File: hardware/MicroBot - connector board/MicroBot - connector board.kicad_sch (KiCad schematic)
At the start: 29 parts, among them J0 SMM_Mega_Shield_Connector, J1 X_Axis_Stepper_Controller, J3 gen4-IB, J4 24VDC, M1 Motor_DC, U1 L9110_H-Bridge, U2 R-78C12-1.0, U3 R-78C12-1.0, U5 OKI-78SR-5_1.5-W36-C

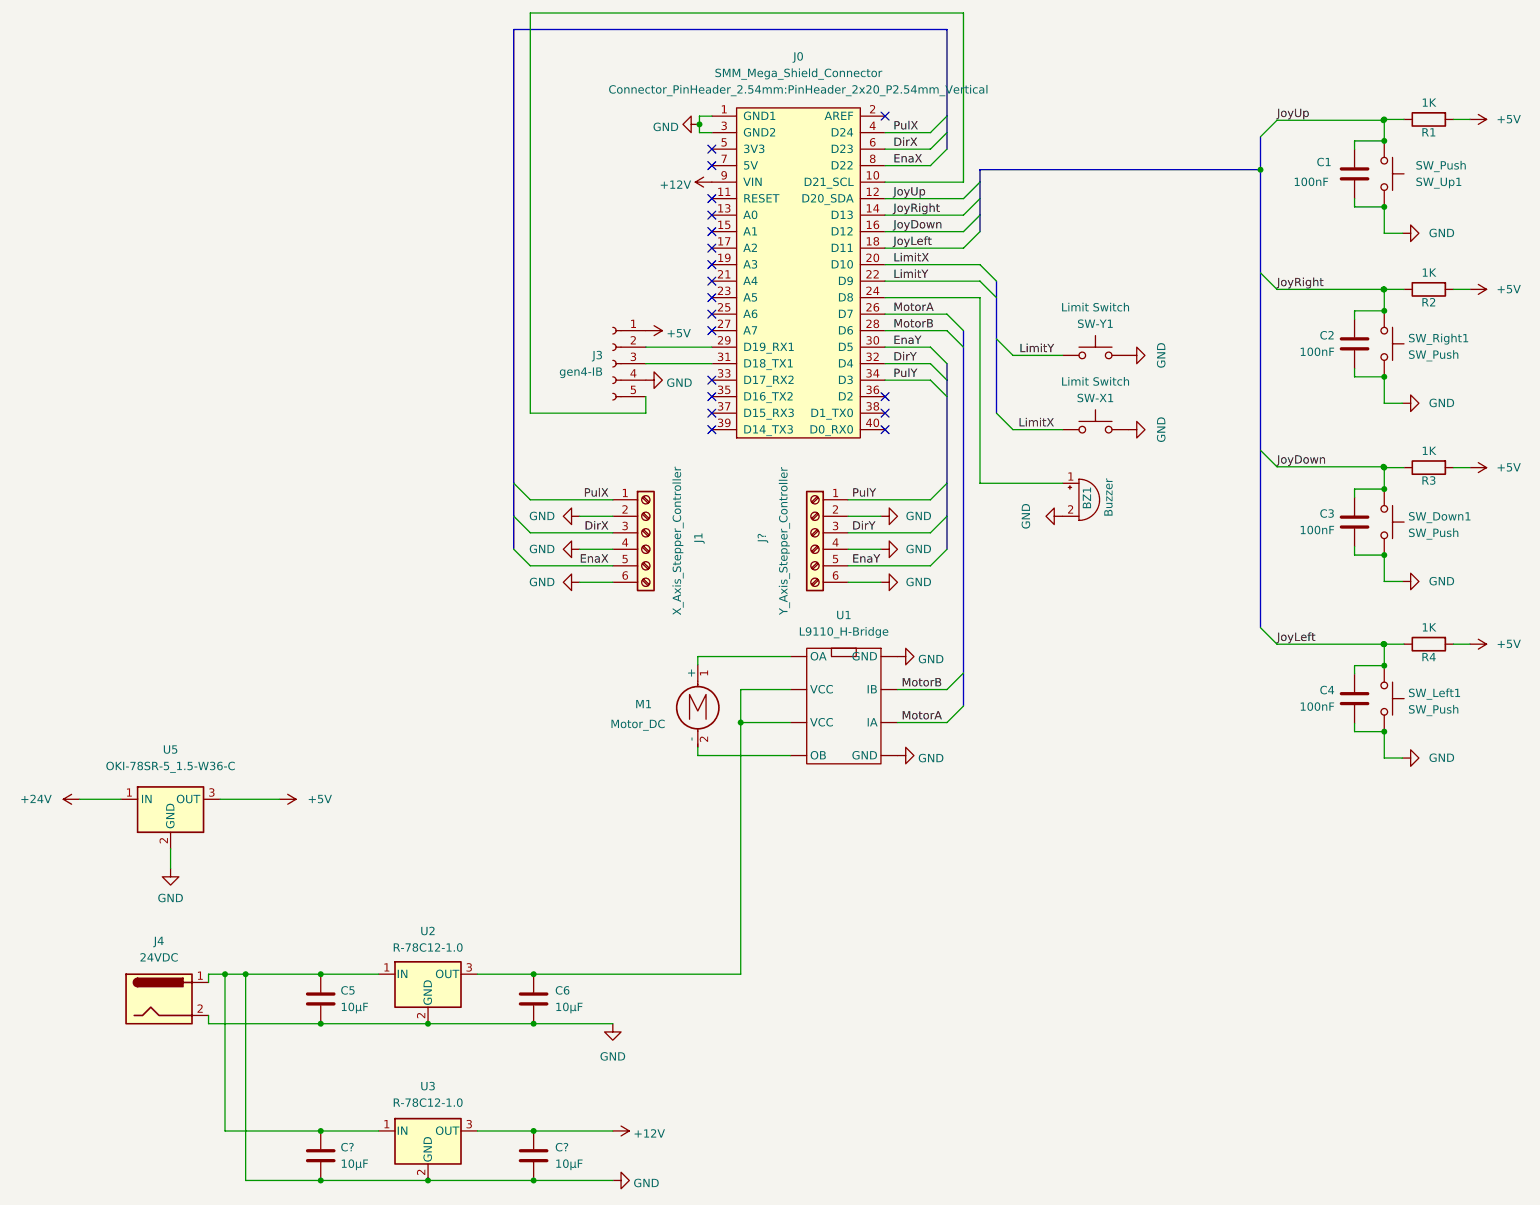
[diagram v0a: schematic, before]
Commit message: add first-pass PCB layout
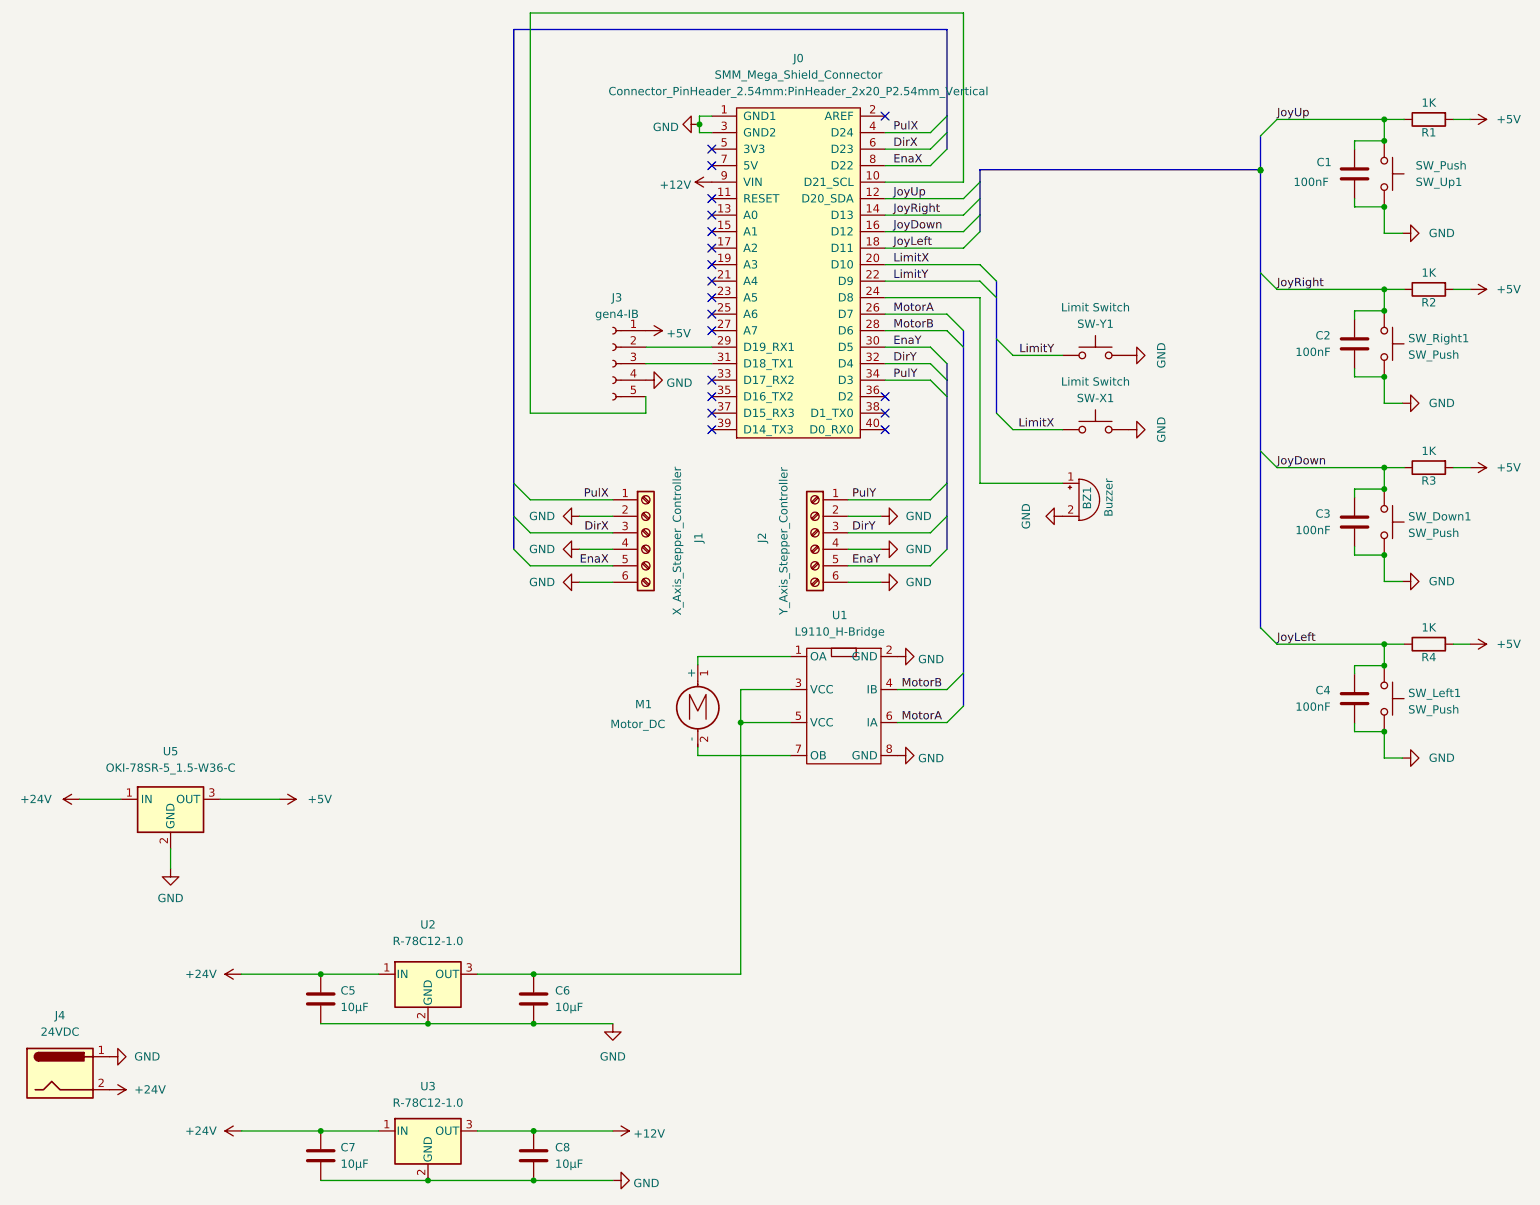
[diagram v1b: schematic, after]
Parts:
- C1, C2, C3, C4: footprint Capacitor_THT:CP_Radial_D4.0mm_P1.50mm -> Capacitor_THT:C_Disc_D3.0mm_W2.0mm_P2.50mm
- J1: footprint (none) -> TerminalBlock:TerminalBlock_bornier-6_P5.08mm
- J2: renamed from J?; footprint (none) -> TerminalBlock:TerminalBlock_bornier-6_P5.08mm
- J3: footprint SMM:I50115 -> Connector_PinSocket_2.54mm:PinSocket_1x05_P2.54mm_Horizontal
- U1: footprint Package_DIP:DIP-8-16_W7.62mm_Socket -> Package_DIP:DIP-8_W7.62mm_Socket
- gave numbers to parts that had none: 2
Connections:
- net +24V: now also C5.1, C7.1, J4.2, U2.1 (IN), U3.1 (IN)
- net GND: now also U1.2 (GND), U1.8 (GND); no longer C5.1, C7.1, J4.2, U1. (VCC), U2.1 (IN), U3.1 (IN)
- net JoyDown: now also C3.2, R3.1, SW_Down1.2
- net JoyLeft: now also C4.2, R4.1, SW_Left1.2
- net JoyRight: now also C2.2, R2.1, SW_Right1.2
- net JoyUp: now also C1.2, R1.1, SW_Up1.2
- net MotorA: now also U1.6 (IA); no longer U1. (VCC)
- net MotorB: now also U1.4 (IB); no longer U1. (VCC)
- net at M1.1 (+): now also U1.1 (OA); no longer U1. (VCC)
- net at M1.2 (-): now also U1.7 (OB); no longer U1. (VCC)
- net at C6.1, U2.3 (OUT): now also U1.3 (VCC), U1.5 (VCC); no longer U1. (VCC)
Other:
- moved on the sheet: J4

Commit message: finalize board layout
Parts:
- added D1: LED, SMM:LED_D3.0mm, symbol Device:LED
- added R5: R, SMM:Resistor_L6.3mm_D2.5mm_P10.16mm_Horizontal, symbol Device:R
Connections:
- net +5V: now also D1.2 (A)
- net GND: now also R5.2
- new net: D1.1 (K), R5.1
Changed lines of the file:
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@@
+    (pin "2")
+  )
+  (symbol (lib_id "Device:LED") (at 177.927 137.795 90) (unit 1)
+    (in_bom yes) (on_board yes) (fields_autoplaced)
+    (property "Reference" "D1" (id 0) (at 181.61 138.1124 90)
+      (effects (font (size 1.27 1.27)) (justify right))
+    )
+    (property "Value" "LED" (id 1) (at 181.61 140.6524 90)
+      (effects (font (size 1.27 1.27)) (justify right))
+    )
+    (property "Footprint" "SMM:LED_D3.0mm" (id 2) (at 177.927 137.795 0)
+      (effects (font (size 1.27 1.27)) hide)
+    )
+    (property "Datasheet" "~" (id 3) (at 177.927 137.795 0)
+      (effects (font (size 1.27 1.27)) hide)
+    )
+    (pin "1")
     (pin "2")
   )
@@
     )
     (property "Datasheet" "" (id 3) (at 149.225 103.505 0)
+      (effects (font (size 1.27 1.27)) hide)
+    )
+    (pin "1")
+  )
+  (symbol (lib_id "power:GND") (at 177.927 149.225 0) (unit 1)
+    (in_bom yes) (on_board yes) (fields_autoplaced)
+    (property "Reference" "#PWR016" (id 0) (at 177.927 155.575 0)
+      (effects (font (size 1.27 1.27)) hide)
+    )
+    (property "Value" "GND" (id 1) (at 177.927 153.67 0))
+    (property "Footprint" "" (id 2) (at 177.927 149.225 0)
+      (effects (font (size 1.27 1.27)) hide)
+    )
+    (property "Datasheet" "" (id 3) (at 177.927 149.225 0)
       (effects (font (size 1.27 1.27)) hide)
     )
@@
     (pin "2")
   )
+  (symbol (lib_id "power:+5V") (at 177.927 133.985 0) (unit 1)
+    (in_bom yes) (on_board yes) (fields_autoplaced)
+    (property "Reference" "#PWR015" (id 0) (at 177.927 137.795 0)
+      (effects (font (size 1.27 1.27)) hide)
+    )
+    (property "Value" "+5V" (id 1) (at 177.927 128.27 0))
+    (property "Footprint" "" (id 2) (at 177.927 133.985 0)
+      (effects (font (size 1.27 1.27)) hide)
+    )
+    (property "Datasheet" "" (id 3) (at 177.927 133.985 0)
+      (effects (font (size 1.27 1.27)) hide)
+    )
+    (pin "1")
+  )
   (symbol (lib_id "Connector:Screw_Terminal_01x06") (at 113.03 95.885 0) (unit 1)
     (in_bom yes) (on_board yes)
@@
     (pin "1")
   )
+  (symbol (lib_id "Device:R") (at 177.927 145.415 0) (unit 1)
+    (in_bom yes) (on_board yes) (fields_autoplaced)
+    (property "Reference" "R5" (id 0) (at 180.34 144.1449 0)
+      (effects (font (size 1.27 1.27)) (justify left))
+    )
+    (property "Value" "R" (id 1) (at 180.34 146.6849 0)
+      (effects (font (size 1.27 1.27)) (justify left))
+    )
+    (property "Footprint" "SMM:Resistor_L6.3mm_D2.5mm_P10.16mm_Horizontal" (id 2) (at 176.149 145.415 90)
+      (effects (font (size 1.27 1.27)) hide)
+    )
+    (property "Datasheet" "~" (id 3) (at 177.927 145.415 0)
+      (effects (font (size 1.27 1.27)) hide)
+    )
+    (pin "1")
+    (pin "2")
+  )
   (symbol (lib_id "power:GND") (at 229.489 75.946 90) (mirror x) (unit 1)
     (in_bom yes) (on_board yes) (fields_autoplaced)
@@
       (reference "#PWR014") (unit 1) (value "GND") (footprint "")
     )
+    (path "/c90f9f6a-5ba5-4e90-a36c-e181972e485f"
+      (reference "#PWR015") (unit 1) (value "+5V") (footprint "")
+    )
+    (path "/15186413-bac9-4c4a-a393-6697a203cfc2"
+      (reference "#PWR016") (unit 1) (value "GND") (footprint "")
+    )
     (path "/2d62c43b-bbf2-4b5c-8cbd-bda299b98654"
       (reference "#PWR0101") (unit 1) (value "+5V") (footprint "")
@@
       (reference "C8") (unit 1) (value "10µF") (footprint "Capacitor_THT:CP_Radial_D4.0mm_P1.50mm")
     )
+    (path "/0fedbe39-d937-427c-8b3c-c6565775d49f"
+      (reference "D1") (unit 1) (value "LED") (footprint "SMM:LED_D3.0mm")
+    )
     (path "/8cf7d650-0997-40ed-ba86-7eb9a2ea678a"
       (reference "J0") (unit 1) (value "SMM_Mega_Shield_Connector") (footprint "Connector_PinHeader_2.54mm:PinHeader_2x20_P2.54mm_Vertical")
@@
       (reference "R4") (unit 1) (value "1K") (footprint "SMM:Resistor_L6.3mm_D2.5mm_P10.16mm_Horizontal")
     )
+    (path "/ec3c3601-267b-4ac6-9565-a5027e901a64"
+      (reference "R5") (unit 1) (value "R") (footprint "SMM:Resistor_L6.3mm_D2.5mm_P10.16mm_Horizontal")
+    )
     (path "/67da5344-8db8-4d0f-b06a-cb5107ffe226"

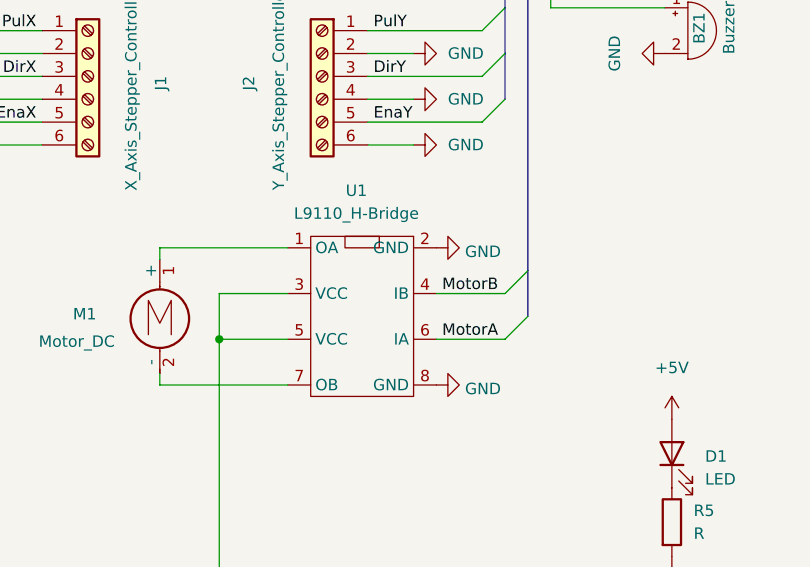
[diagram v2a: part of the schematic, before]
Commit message: fix error in PCB layout
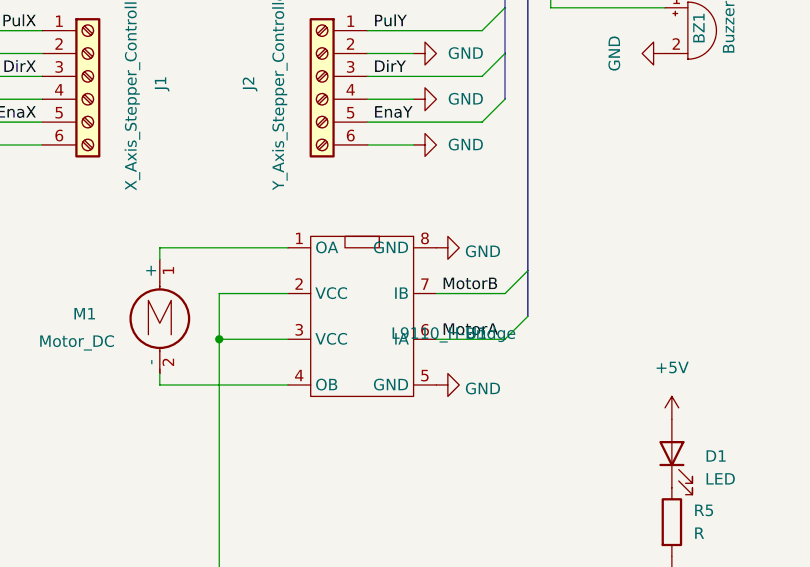
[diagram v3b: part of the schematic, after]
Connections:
- net GND: now also U1.5 (GND); no longer U1.2 (GND)
- net MotorB: now also U1.7 (IB); no longer U1.4 (IB)
- net at M1.2 (-): now also U1.4 (OB); no longer U1.7 (OB)
- net at C6.1, U1.3 (VCC), U2.3 (OUT): now also U1.2 (VCC); no longer U1.5 (VCC)
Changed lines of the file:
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@@
   (symbol (lib_id "L9110 H-Bridge:L9110_H-Bridge") (at 141.605 122.555 270) (unit 1)
     (in_bom yes) (on_board yes) (fields_autoplaced)
-    (property "Reference" "U1" (id 0) (at 142.875 108.585 90))
-    (property "Value" "L9110_H-Bridge" (id 1) (at 142.875 111.125 90))
+    (property "Reference" "U1" (id 0) (at 156.21 124.46 90))
+    (property "Value" "L9110_H-Bridge" (id 1) (at 153.67 124.46 90))
     (property "Footprint" "Package_DIP:DIP-8_W7.62mm_Socket" (id 2) (at 141.605 122.555 0)
       (effects (font (size 1.27 1.27)) hide)
@@
       (effects (font (size 1.27 1.27)) hide)
     )
+    (pin "1")
+    (pin "8")
     (pin "2")
-    (pin "8")
+    (pin "7")
+    (pin "3")
     (pin "6")
     (pin "4")
-    (pin "1")
-    (pin "7")
-    (pin "3")
     (pin "5")
   )
